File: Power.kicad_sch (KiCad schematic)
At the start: 56 parts, among them J2 Charge, J3 Battery, Q1 AO3401A, Q2 AO3400A, Q3 AO3401A, U4 FUSB303BTMX, U5 TPS61089, U6 D3V3XA4B10LP, U7 BQ25895RTW, U8 TPS63001

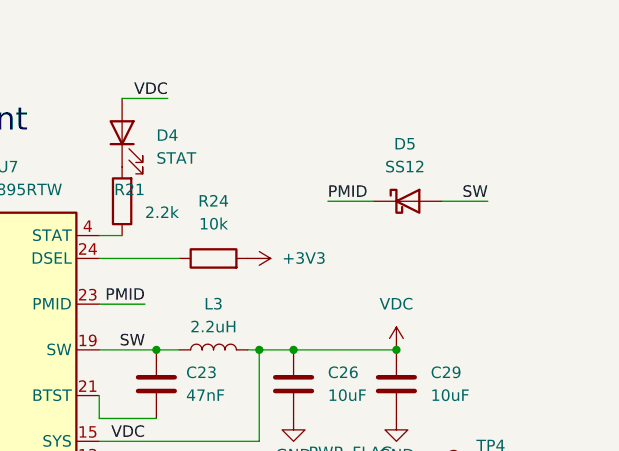
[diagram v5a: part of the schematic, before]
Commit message: Optimize Cryobelt JLC assembly parts
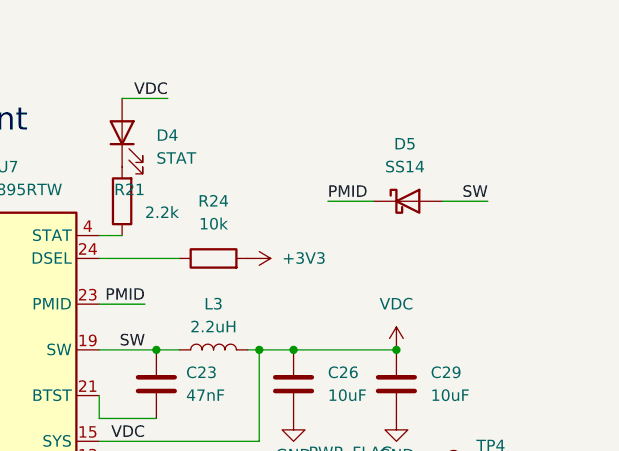
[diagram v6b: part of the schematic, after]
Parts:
- C14: LCSC Part # C86295 -> C59461; MPN CL10A226MP8NUNE -> CL10A226MQ8NRNC
- C19: Manufacturer YAGEO -> FH (Guangdong Fenghua Advanced Tech)
- D5: value SS12 -> SS14; LCSC Part # C184027 -> C2480; MPN SS12 -> SS14; Manufacturer onsemi -> MDD (Microdiode Semiconductor)
- L1, L3: footprint Cryobelt:FEXU0420 -> Inductor_SMD:L_Changjiang_FNR4030S
- L2: footprint Inductor_SMD:L_APV_ANR4020 -> Inductor_SMD:L_Changjiang_FNR4030S; LCSC Part # C135262 -> C54777963; MPN SMNR4020-2.2UH -> FEXU0420S2R2MBS; Manufacturer Shun Xiang Nuo -> cjiang
- R11, R13: Manufacturer YAGEO -> UNI-ROYAL
- R22: LCSC Part # C137745 -> C22984; Manufacturer YAGEO -> UNI-ROYAL
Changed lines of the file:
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@@
 			)
 		)
-		(property "Manufacturer" "YAGEO"
+ (property "Manufacturer" "UNI-ROYAL"
 			(at 0 0 0)
 			(hide yes)
@@
 			)
 		)
-		(property "LCSC Part #" "C137745"
+		(property "LCSC Part #" "C22984"
 			(at 0 0 0)
 			(hide yes)
@@
 			)
 		)
-		(property "MPN" "CL10A226MP8NUNE"
+		(property "MPN" "CL10A226MQ8NRNC"
 			(at 0 0 0)
 			(hide yes)
@@
 			)
 		)
-		(property "LCSC Part #" "C86295"
+		(property "LCSC Part #" "C59461"
 			(at 0 0 0)
 			(hide yes)
@@
 			)
 		)
-		(property "Value" "SS12"
+		(property "Value" "SS14"
 			(at 262.5725 26.67 0)
 			(show_name no)
@@
 			)
 		)
-		(property "Datasheet" "https://www.vishay.com/docs/88746/ss12.pdf"
+		(property "Datasheet" "https://www.lcsc.com/datasheet/lcsc_datasheet_2407101109_MDD-Microdiode-Semiconductor-SS14_C2480.pdf"
 			(at 262.89 30.48 0)
 			(hide yes)
@@
 			)
 		)
-		(property "Description" "20V 1A Schottky Diode, SMA"
+		(property "Description" "40V 1A Schottky diode, SMA"
 			(at 262.89 30.48 0)
 			(hide yes)
@@
 			)
 		)
-		(property "Manufacturer" "onsemi"
+		(property "Manufacturer" "MDD (Microdiode Semiconductor)"
 			(at 0 0 0)
 			(hide yes)
@@
 			)
 		)
-		(property "MPN" "SS12"
+		(property "MPN" "SS14"
 			(at 0 0 0)
 			(hide yes)
@@
 			)
 		)
-		(property "LCSC Part #" "C184027"
+		(property "LCSC Part #" "C2480"
 			(at 0 0 0)
 			(hide yes)
@@
 			)
 		)
-		(property "Footprint" "Cryobelt:FEXU0420"
+		(property "Footprint" "Inductor_SMD:L_Changjiang_FNR4030S"
 			(at 107.95 132.08 0)
 			(hide yes)
@@
 			)
 		)
-		(property "Footprint" "Cryobelt:FEXU0420"
+		(property "Footprint" "Inductor_SMD:L_Changjiang_FNR4030S"
 			(at 241.3 46.99 0)
 			(hide yes)
@@
 			)
 		)
-		(property "Manufacturer" "YAGEO"
+ (property "Manufacturer" "UNI-ROYAL"
 			(at 0 0 0)
 			(hide yes)
@@
 			)
 		)
-		(property "Footprint" "Inductor_SMD:L_APV_ANR4020"
+		(property "Footprint" "Inductor_SMD:L_Changjiang_FNR4030S"
 			(at 223.52 146.05 0)
 			(hide yes)
@@
 			)
 		)
-		(property "Manufacturer" "Shun Xiang Nuo"
+ (property "Manufacturer" "cjiang"
 			(at 0 0 0)
 			(hide yes)
@@
 			)
 		)
-		(property "MPN" "SMNR4020-2.2UH"
+		(property "MPN" "FEXU0420S2R2MBS"
 			(at 0 0 0)
 			(hide yes)
@@
 			)
 		)
-		(property "LCSC Part #" "C135262"
+		(property "LCSC Part #" "C54777963"
 			(at 0 0 0)
 			(hide yes)
@@
 			)
 		)
-		(property "Manufacturer" "YAGEO"
+ (property "Manufacturer" "FH (Guangdong Fenghua Advanced Tech)"
 			(at 0 0 0)
 			(hide yes)
@@
 			)
 		)
-		(property "Manufacturer" "YAGEO"
+ (property "Manufacturer" "UNI-ROYAL"
 			(at 0 0 0)
 			(hide yes)
